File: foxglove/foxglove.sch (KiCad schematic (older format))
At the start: 24 parts, among them J1 NEIGHBOR1, J2 NEIGHBOR2, J7 BONUS_ROW, U10 iCE40HX4K

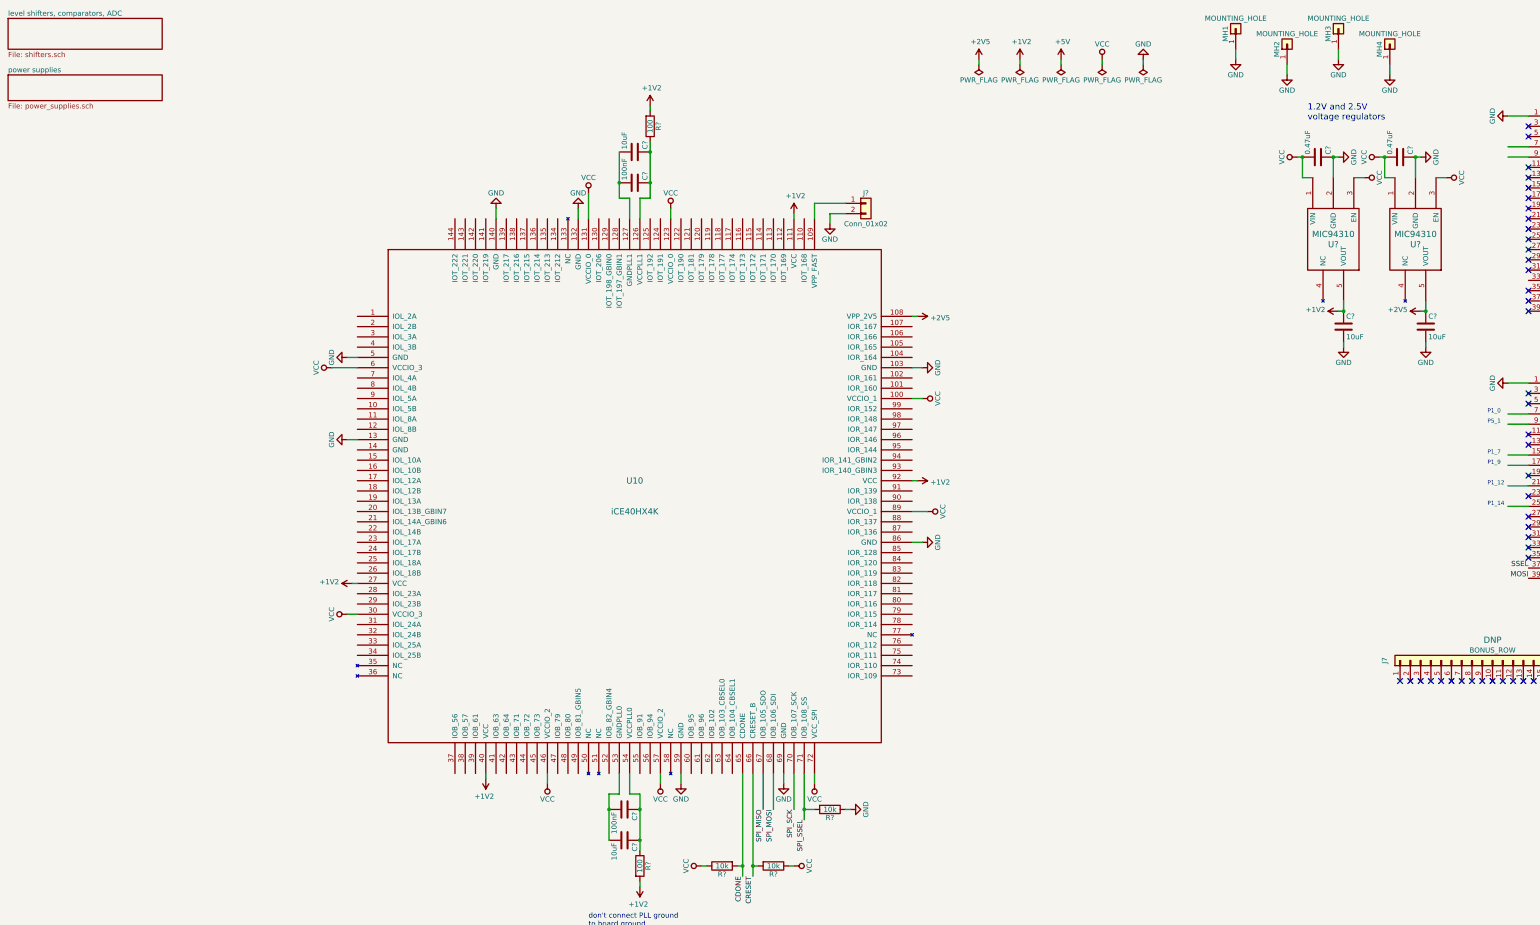
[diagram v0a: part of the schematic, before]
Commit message: Added multiplexors to bank A
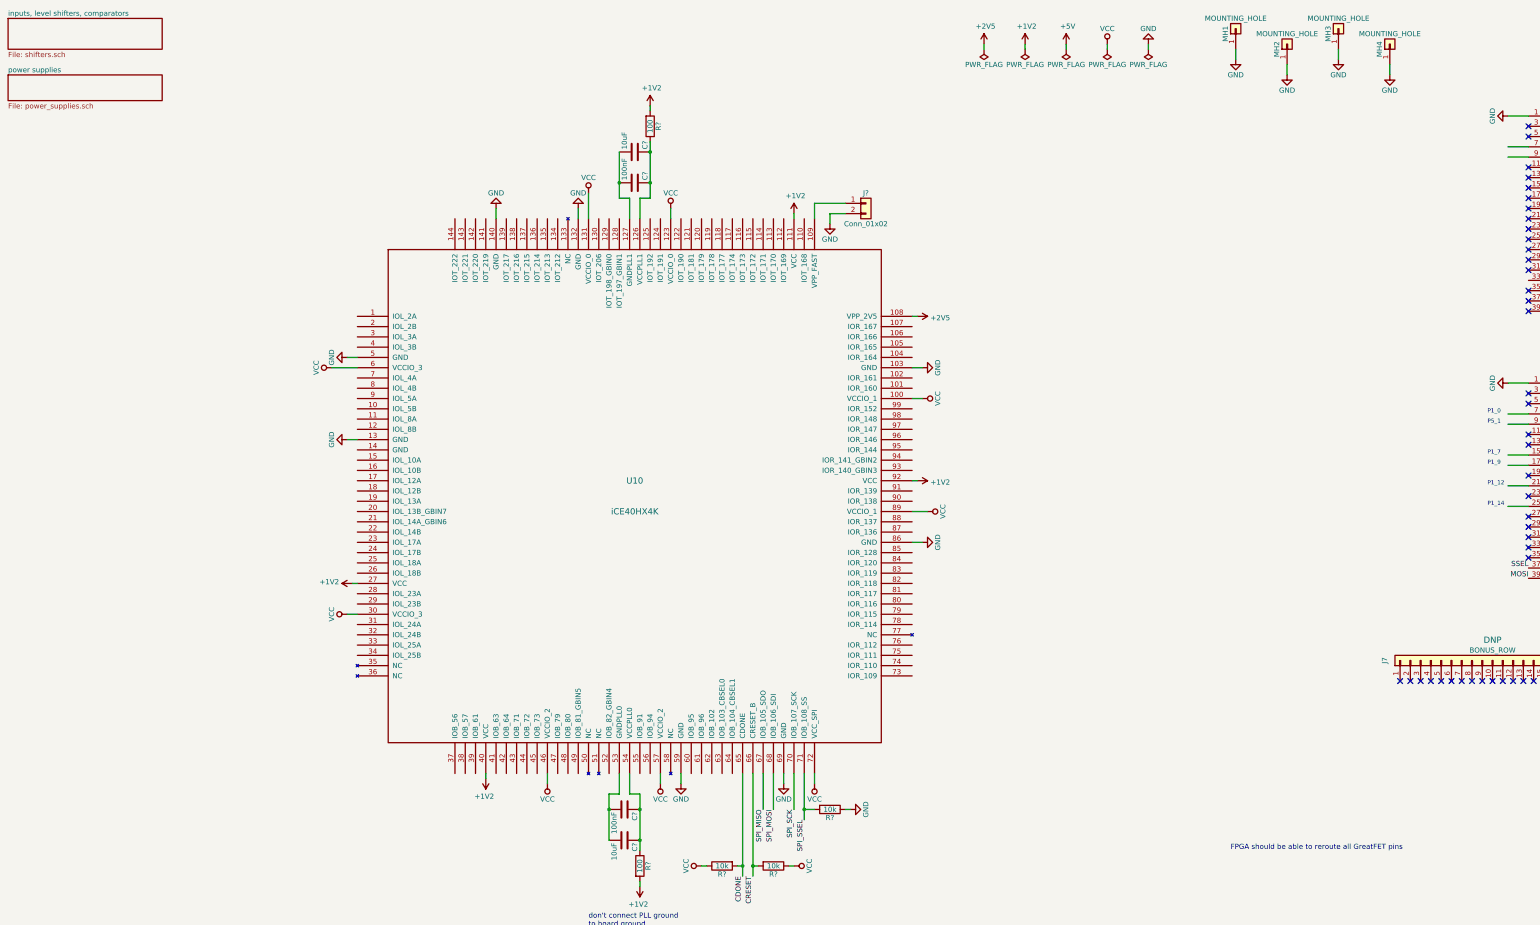
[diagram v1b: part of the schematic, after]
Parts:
- removed C? (x2): 10uF, symbol Device:C
- removed C? (x2): 0.47uF, symbol Device:C
- removed U? (x2): MIC94310, symbol gsg-symbols:MIC94310
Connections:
- wire segments 114 -> 96
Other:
- note added: "FPGA should be able to reroute all GreatFET pins"
- note removed: "1.2V and 2.5V\nvoltage regulators"

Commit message: Added ice40 symbol
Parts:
- added U? (x5): ICE40HX8K-BG121, Package_BGA:BGA-121_9.0x9.0mm_Layout11x11_P0.8mm_Ball0.4mm_Pad0.35mm_NSMD, symbol FPGA_Lattice:ICE40HX8K-BG121
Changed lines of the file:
@@
 Text Notes 12600 8850 0    50   ~ 0
 FPGA should be able to reroute all GreatFET pins
+$Comp
+L FPGA_Lattice:ICE40HX8K-BG121 U?
+U 1 1 5C916766
+P -3200 7950
+F 0 "U?" H -2820 7952 50  0000 L CNN
+F 1 "ICE40HX8K-BG121" H -2820 7861 50  0000 L CNN
+F 2 "Package_BGA:BGA-121_9.0x9.0mm_Layout11x11_P0.8mm_Ball0.4mm_Pad0.35mm_NSMD" H -3200 6500 50  0001 C CNN
+F 3 "http://www.latticesemi.com/Products/FPGAandCPLD/iCE40" H -4050 8950 50  0001 C CNN
+	1    -3200 7950
+	1    0    0    -1
+$EndComp
+$Comp
+L FPGA_Lattice:ICE40HX8K-BG121 U?
+U 2 1 5C916ABB
+P -1550 8050
+F 0 "U?" H -1170 8152 50  0000 L CNN
+F 1 "ICE40HX8K-BG121" H -1170 8061 50  0000 L CNN
+F 2 "Package_BGA:BGA-121_9.0x9.0mm_Layout11x11_P0.8mm_Ball0.4mm_Pad0.35mm_NSMD" H -1550 6600 50  0001 C CNN
+F 3 "http://www.latticesemi.com/Products/FPGAandCPLD/iCE40" H -2400 9050 50  0001 C CNN
+	2    -1550 8050
+	1    0    0    -1
+$EndComp
+$Comp
+L FPGA_Lattice:ICE40HX8K-BG121 U?
+U 5 1 5C916D12
+P -3000 13300
+F 0 "U?" H -3000 12514 50  0000 C CNN
+F 1 "ICE40HX8K-BG121" H -3000 12423 50  0000 C CNN
+F 2 "Package_BGA:BGA-121_9.0x9.0mm_Layout11x11_P0.8mm_Ball0.4mm_Pad0.35mm_NSMD" H -3000 11850 50  0001 C CNN
+F 3 "http://www.latticesemi.com/Products/FPGAandCPLD/iCE40" H -3850 14300 50  0001 C CNN
+	5    -3000 13300
+	1    0    0    -1
+$EndComp
+$Comp
+L FPGA_Lattice:ICE40HX8K-BG121 U?
+U 3 1 5C91BA00
+P -3250 10900
+F 0 "U?" H -3250 9576 50  0000 C CNN
+F 1 "ICE40HX8K-BG121" H -3250 9485 50  0000 C CNN
+F 2 "Package_BGA:BGA-121_9.0x9.0mm_Layout11x11_P0.8mm_Ball0.4mm_Pad0.35mm_NSMD" H -3250 9450 50  0001 C CNN
+F 3 "http://www.latticesemi.com/Products/FPGAandCPLD/iCE40" H -4100 11900 50  0001 C CNN
+	3    -3250 10900
+	1    0    0    -1
+$EndComp
+$Comp
+L FPGA_Lattice:ICE40HX8K-BG121 U?
+U 4 1 5C91BD33
+P -1700 11300
+F 0 "U?" H -1320 11427 50  0000 L CNN
+F 1 "ICE40HX8K-BG121" H -1320 11336 50  0000 L CNN
+F 2 "Package_BGA:BGA-121_9.0x9.0mm_Layout11x11_P0.8mm_Ball0.4mm_Pad0.35mm_NSMD" H -1700 9850 50  0001 C CNN
+F 3 "http://www.latticesemi.com/Products/FPGAandCPLD/iCE40" H -2550 12300 50  0001 C CNN
+	4    -1700 11300
+	1    0    0    -1
+$EndComp
 $EndSCHEMATC
